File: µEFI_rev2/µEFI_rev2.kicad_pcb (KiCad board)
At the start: 4 copper layers, 99.9 x 129.8 mm, 194 parts, among them J1 USB_B, J2 Tag connect, J3 36638-0002, J4 Conn_02x08_Odd_Even, Q1 ISL9V5045S3ST, Q10 IRF540N, Q11 SS8050, Q12 AO3400A, Q2 ISL9V5045S3ST, Q3 ISL9V5045S3ST, Q4 ISL9V5045S3ST, Q5 SS8050, Q6 IRF540N, Q7 IRF540N, Q8 SS8050, Q9 SS8050, SW1 SW_Push, U1 MCZ33810EK, U10 SensorsV2, U11 SensorsV2, U12 SensorsV2, U13 SensorsV2, U14 SensorsV2, U15 TJA1042T3118, U2 SensorsV2, U20 TPL7407LAPWR, U22 TPL7407LAPWR, U23 PaP_Driver_v1, U27 LM321, U3 STM32F407VGTx, U31 LM321, U36 MAX9926UAEE+, U4 MIC2940A-3.3WU, U5 MIC2940A-5.0WT, U6 LT4363IMS, U7 25LCxxx, U8 SensorsV2, U9 SensorsV2, Y1 25MHz

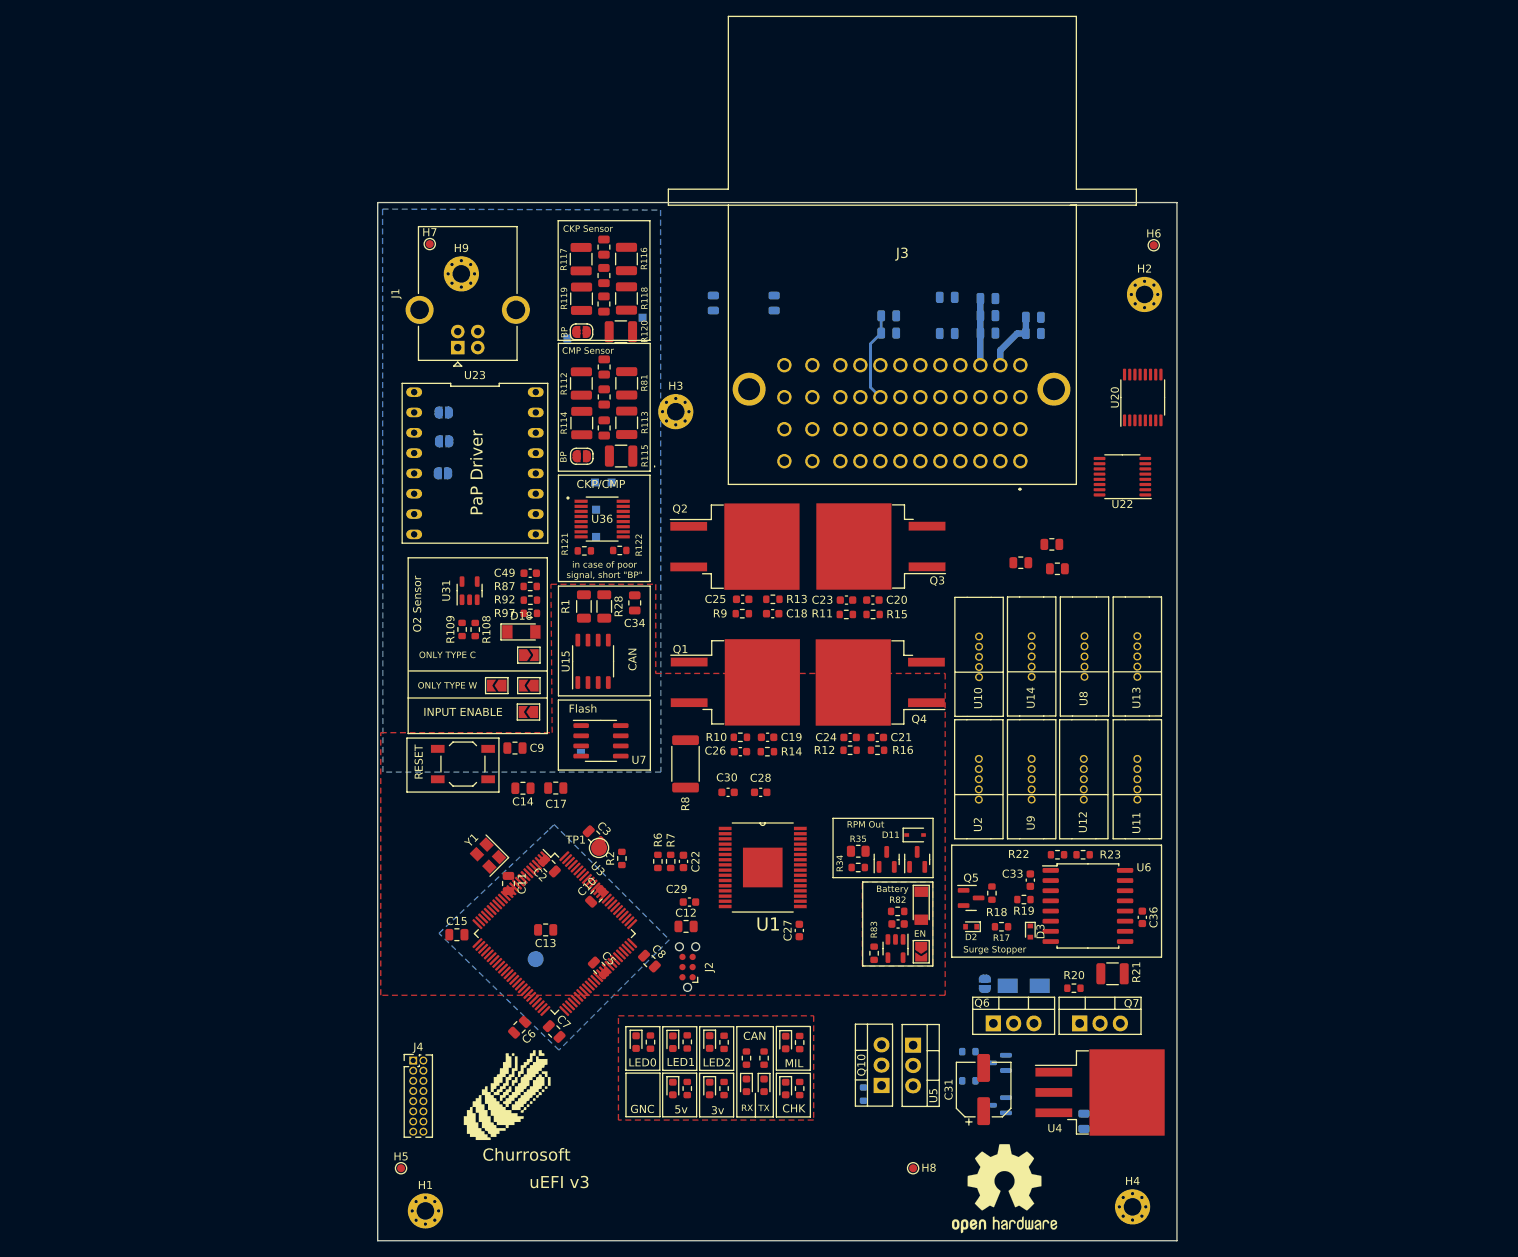
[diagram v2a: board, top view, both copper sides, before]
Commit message: move old boards to __old
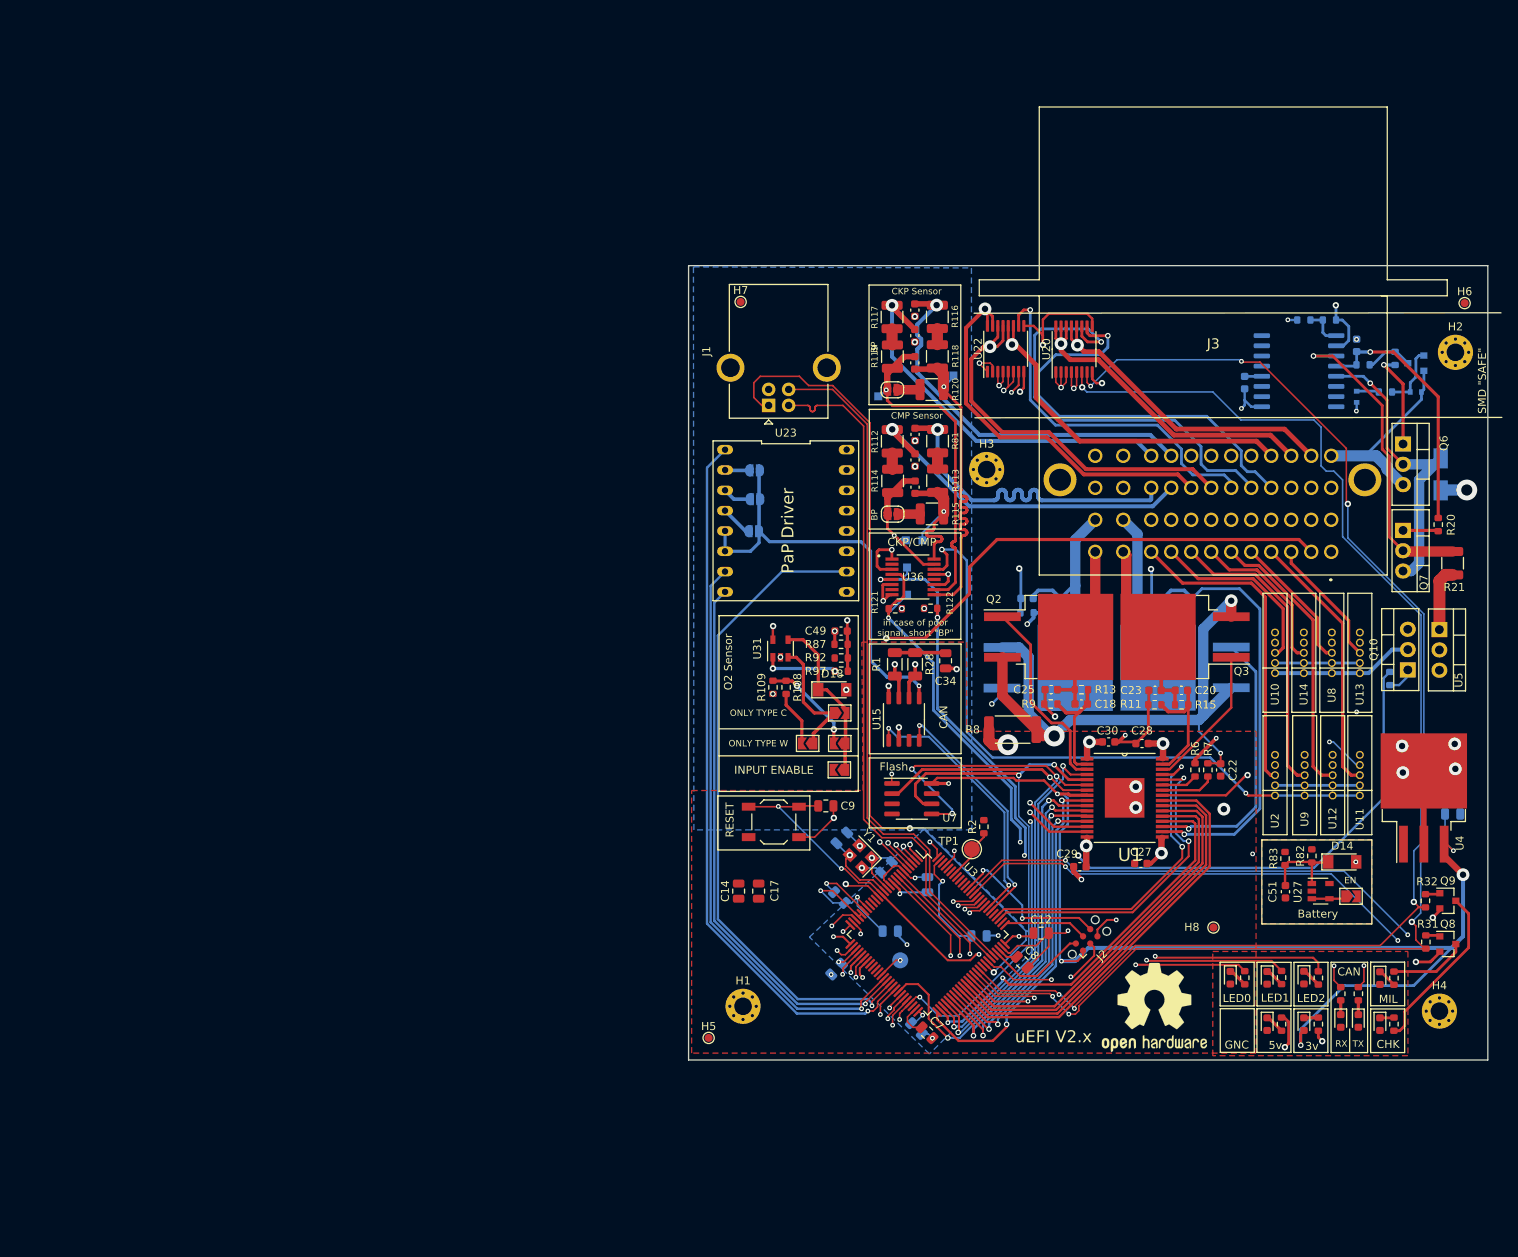
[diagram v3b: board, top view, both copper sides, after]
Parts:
- removed C31: 100uF ±20% 35V, Capacitor_SMD:CP_Elec_6.3x7.7
- removed Churrosoft: SYM_Hot_Large, OpenEFI-STM32F_rev3:churro_new_v4
- removed D11: MM3Z24VT1G, Diode_SMD:D_SOD-323
- removed F1, F10, F11, F12, F13, F14, F2, F3, F4, F5, F6, F7, F8, F9: 750mA, Fuse:Fuse_0805_2012Metric
- removed H9: MountingHole, MountingHole:MountingHole_2.2mm_M2_Pad_Via
- removed J4: Conn_02x08_Odd_Even, Connector_PinHeader_1.27mm:PinHeader_2x08_P1.27mm_Vertical
- removed JP4: Jumper_NO_Small, Jumper:SolderJumper-2_P1.3mm_Open_RoundedPad1.0x1.5mm
- removed Q11: SS8050, Package_TO_SOT_SMD:SOT-23
- removed Q12: AO3400A, Package_TO_SOT_SMD:SOT-23
- removed R34: 1k, Resistor_SMD:R_0603_1608Metric
- removed R35: 100k, Resistor_SMD:R_0805_2012Metric
- removed TP9: TestPoint, TestPoint:TestPoint_Pad_1.0x1.0mm
- C10, C11, C13, C15, C19, C2, C21, C24, C26, C3, C33, C36, C5, C6, D2, D3, Q1, Q4, Q5, R10, R12, R14, R16, R17, R18, R19, R22, R23, U6: moved to B.Cu
- C52, C53, C54, C55, C56, C57: footprint Capacitor_SMD:C_0805_2012Metric -> Capacitor_SMD:C_0603_1608Metric
- Q8, Q9, R31, R32: moved to F.Cu
- R24, R25, R26, R27, R29, R3, R30, R4, R5: value 4.7k -> R_Small
- moved Q6 88.7 mm to (182.4, 70.8), turned to -90 degrees
- moved D2 86.9 mm to (184.0, 64.3), turned to 0 degrees
- moved Q5 86.9 mm to (184.0, 60.7), turned to 180 degrees
- moved Q10 83.8 mm to (183.0, 99.0)
- moved R33 83.8 mm to (180.8, 100.1)
- moved U5 83.8 mm to (186.9, 94.0)
- moved R18 83.7 mm to (181.4, 60.1)
- moved D4 82.5 mm to (187.1, 74.6), turned to -90 degrees
- moved R17 82.3 mm to (180.2, 64.3), turned to 180 degrees
- moved R19 79.2 mm to (177.4, 60.9), turned to 0 degrees
- moved D3 78.3 mm to (176.6, 64.9)
- moved C33 78.3 mm to (176.6, 58.4)
- moved R22 75.0 mm to (173.2, 55.3), turned to 180 degrees
- moved D7 74.7 mm to (174.6, 142.9)
- moved R24 74.7 mm to (174.6, 139.5)
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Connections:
- J3 pad A2: +5VA -> A2
- J3 pad A3: GND -> A3
- J3 pad B2: +5VA -> B2
- J3 pad B3: GND -> B3
- J3 pad C2: +5VA -> C2
- J3 pad C3: GND -> C3
- J3 pad D2: +5VA -> D2
- J3 pad E2: +5VA -> E2
- J3 pad F2: +5VA -> F2
- J3 pad G2: GND -> G2
- J3 pad H2: GND -> H2
- J3 pad MH1: GND -> unconnected-(J3-PadMH1)
- J3 pad MH2: GND -> unconnected-(J3-PadMH2)
- U20 pad 10: /PWM/Relays/MIL_OUT -> D3
- U20 pad 11: /PWM/Relays/CHECK_ENGINE -> E3
- U20 pad 12: Net-(U20-Pad12) -> B4
- U20 pad 13: Net-(U20-Pad13) -> B4
- U20 pad 14: Net-(U20-Pad14) -> C4
- U20 pad 15: Net-(U20-Pad15) -> C4
- U20 pad 16: Net-(U20-Pad16) -> C4
- U22 pad 10: /PWM/Relays/R3_OUT -> F3
- U22 pad 11: Net-(U22-Pad11) -> D4
- U22 pad 12: Net-(U22-Pad12) -> D4
- U22 pad 13: Net-(U22-Pad13) -> G3
- U22 pad 14: Net-(U22-Pad14) -> G3
- U22 pad 15: Net-(U22-Pad15) -> H3
- U22 pad 16: Net-(U22-Pad16) -> H3
- U3 pad 15: /Sensores/PC0 -> 5V_ENABLE
- U3 pad 16: 5V_ENABLE -> unconnected-(U3-Pad16)
- U3 pad 18: /AUX_OUT_2 -> unconnected-(U3-Pad18)
- U3 pad 33: /AUX_OUT_1 -> unconnected-(U3-Pad33)
- U3 pad 34: /Sensores/PC5 -> unconnected-(U3-Pad34)
- U3 pad 35: /AUX_OUT_3 -> unconnected-(U3-Pad35)
- U3 pad 91: unconnected-(U3-Pad91) -> /MTR_M_2
- U3 pad 92: unconnected-(U3-Pad92) -> /MTR_M1
- U3 pad 93: unconnected-(U3-Pad93) -> /PAP_ENABLE
- U3 pad 95: unconnected-(U3-Pad95) -> /PWM_ENABLE_2
- U3 pad 96: unconnected-(U3-Pad96) -> /PWM_ENABLE_1
- U7 pad 3: +3V3 -> unconnected-(U7-Pad3)
- U7 pad 7: +3V3 -> unconnected-(U7-Pad7)
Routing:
- net +3V3: track 0.00 -> 265.6 mm, vias 0 -> 15
- net +12V: track 0.00 -> 253.3 mm, vias 0 -> 4
- net GND: track 0.00 -> 191.6 mm, vias 0 -> 53
- net /MIL_OUT: track 0.00 -> 170.0 mm, vias 0 -> 6
- net /CHK_OUT: track 0.00 -> 164.2 mm, vias 0 -> 4
- net +5VA: track 0.00 -> 127.5 mm, vias 0 -> 4
- net /VBUS: track 0.00 -> 104.3 mm, vias 0 -> 2
- net /Sensores/PA7: track 0.00 -> 98.2 mm, vias 0 -> 2
- net /TIM9_CH2: track 0.00 -> 97.2 mm, vias 0 -> 2
- net /TIM9_CH1: track 0.00 -> 96.5 mm, vias 0 -> 2
- net 5V_ENABLE: track 0.00 -> 94.6 mm, vias 0 -> 2
- net /Sensores/PA6: track 0.00 -> 94.0 mm, vias 0 -> 1
- net /MTR_ENABLE: track 0.00 -> 89.8 mm, vias 0 -> 1
- net /R_LMB: track 0.00 -> 89.5 mm, vias 0 -> 2
- net /Sensores/PA3: track 0.00 -> 87.3 mm, vias 0 -> 1
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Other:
- board size 99.9 x 129.8 mm -> 99.9 x 99.3 mm
- board text added: "Aca podria ir otro soporte, pero de plastico, tipo trabita"
- board text added: "Aca va a ir un header con todos los pines que esten al pedo y sirvan para hacer de expansora"
- board text added: "Alimentacion sensores:"
- board text added: "Faltan los caps elec[..] para filtrar el ruido, tambien ceramicos / tantalio"
- board text added: "SMD {dblquote}SAFE{dblquote}"
- board text added: "Salida tacometro"
- board text added: "uEFI V2.x"
- board text removed: "De aca puedo sacar 12v para detectar ACC"
- board text removed: "Esta parte del conector tiene que quedar afuera del pcb:"
- board text removed: "JLCJLCJLCJLC"
- board text removed: "Lote:"
- board text removed: "Mover"
- board text removed: "Notes:"
- board text removed: "PWM0"
- board text removed: "PWM1"
- board text removed: "RPM Out"
- board text removed: "Rev:"
- board text removed: "uEFI v3"
